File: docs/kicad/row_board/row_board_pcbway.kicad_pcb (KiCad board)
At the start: 2 copper layers, 197 x 25 mm, 23 parts, among them J1 Conn_01x06, J2 Conn_01x06, SW1 SW1, SW2 SW1, SW3 SW1, SW4 SW1, SW5 SW1, U1 74HC595

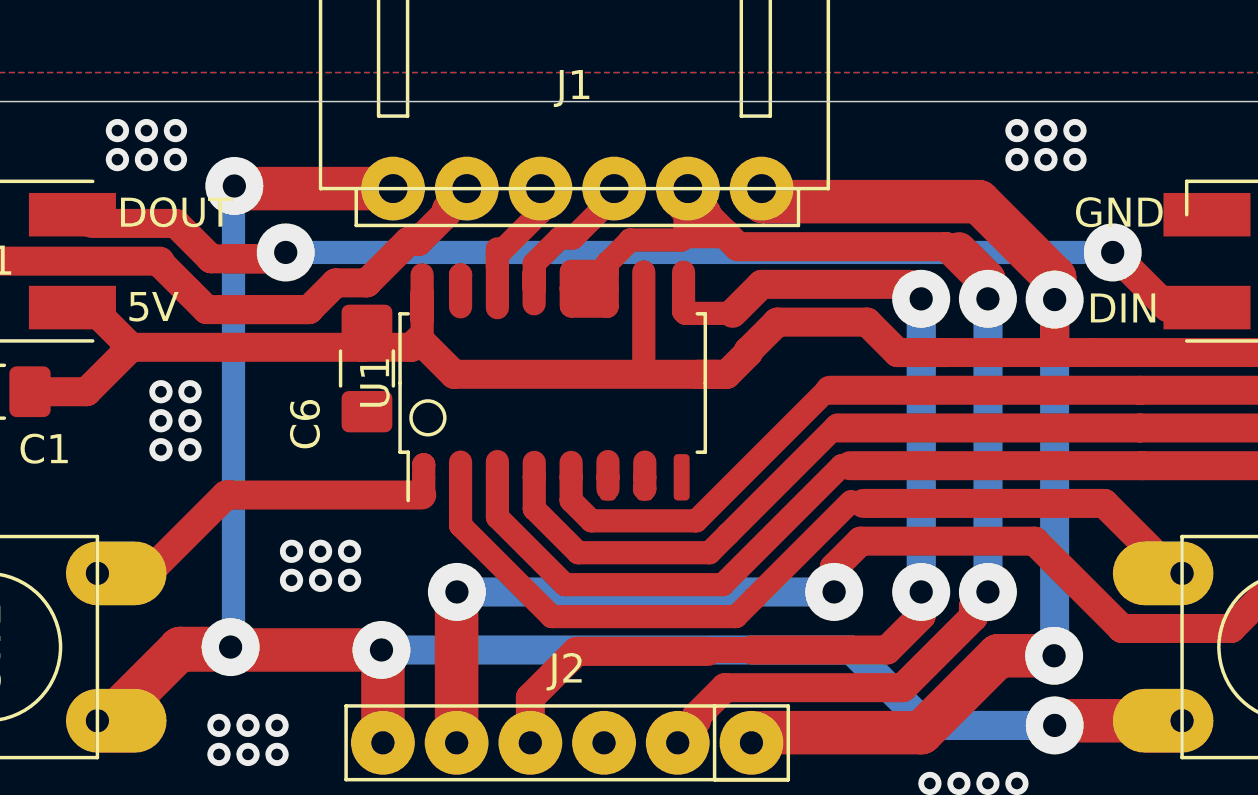
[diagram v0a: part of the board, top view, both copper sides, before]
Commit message: updated PCBWay designs after DRC Design Rules Checks
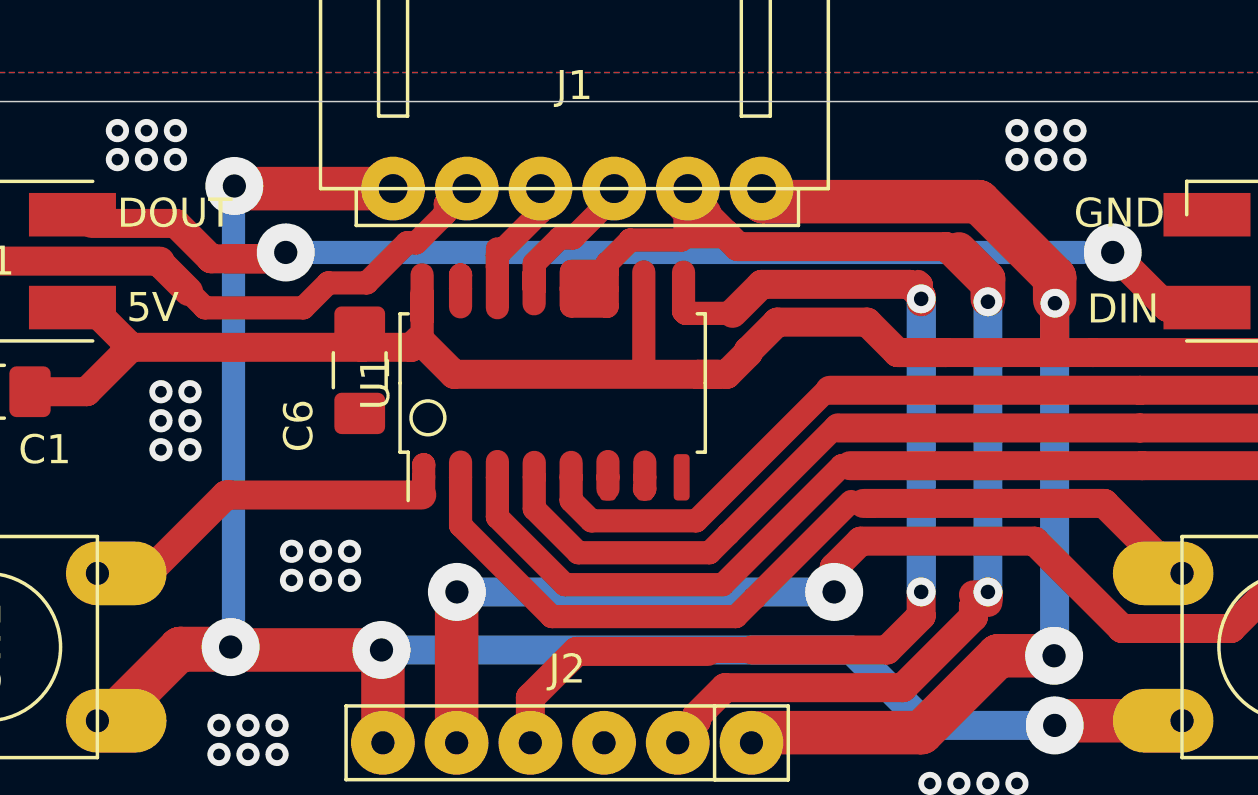
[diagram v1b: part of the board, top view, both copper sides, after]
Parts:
- moved C6 0.26 mm to (72.8, 84.3)
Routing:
- net LED_DIN: track 27.2 -> 24.2 mm
